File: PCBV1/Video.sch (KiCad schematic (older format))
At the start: 0 parts

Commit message: Made comments and some circuits.
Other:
- note added: "Place parallel LCD to HDMI circuits. \n\nBest option: TFP410\n\nPossible ICs:\nSI9022\nADV7513/ADV7511"
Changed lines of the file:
@@
 $Descr A4 11693 8268
 encoding utf-8
-Sheet 1 9
+Sheet 5 8
 Title "Smart Mirror"
 Date "2021-01-21"
@@
 Comment4 ""
 $EndDescr
+Text Notes 4650 3750 0    50   ~ 0
+Place parallel LCD to HDMI circuits. \n\nBest option: TFP410\n\nPossible ICs:\nSI9022\nADV7513/ADV7511
 $EndSCHEMATC

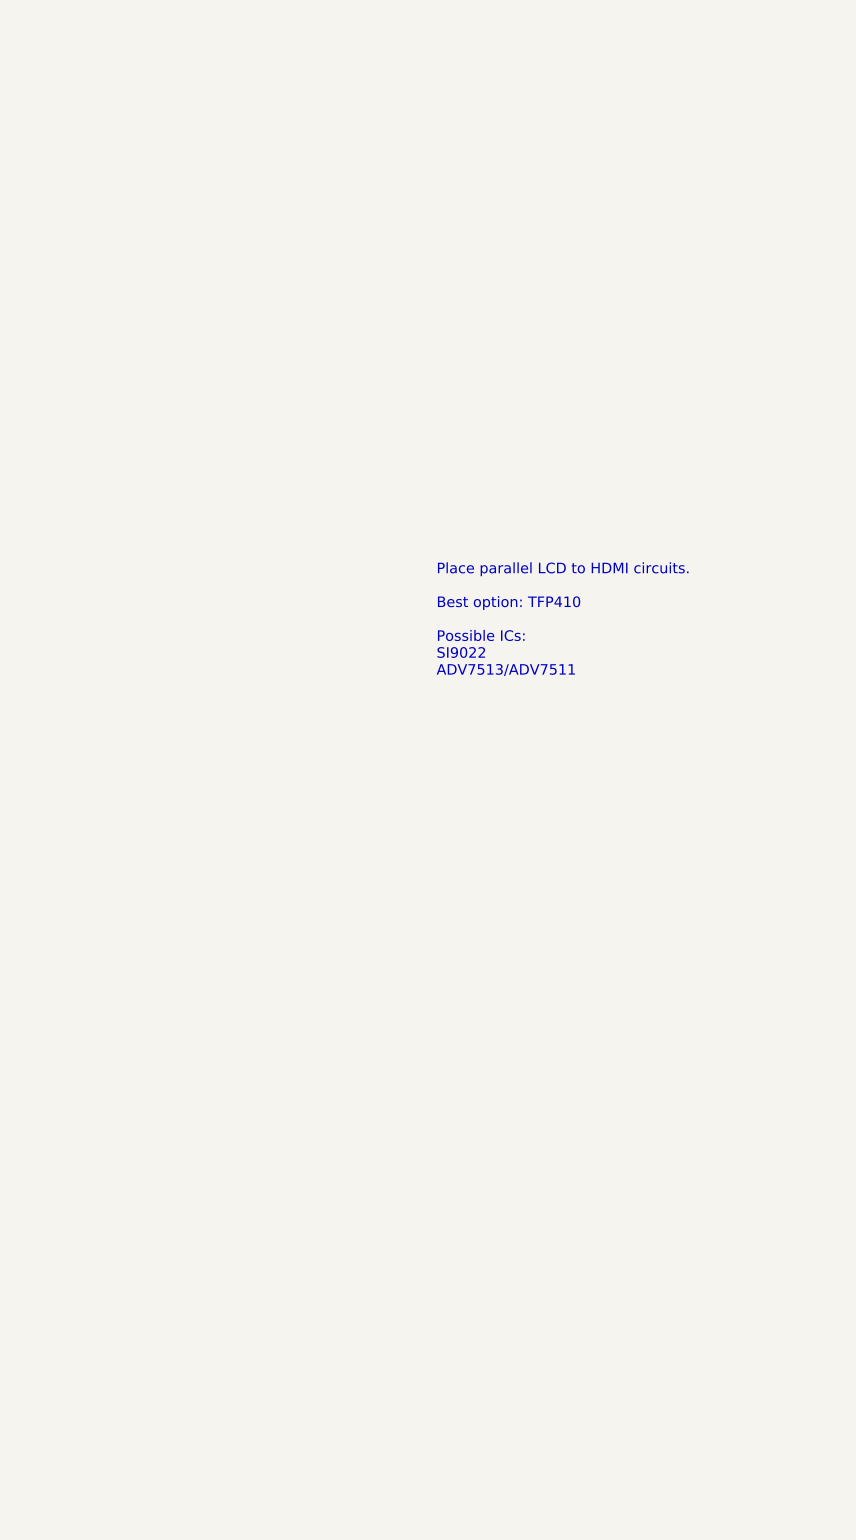
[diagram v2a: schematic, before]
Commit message: Added UART, modifications to video etc.
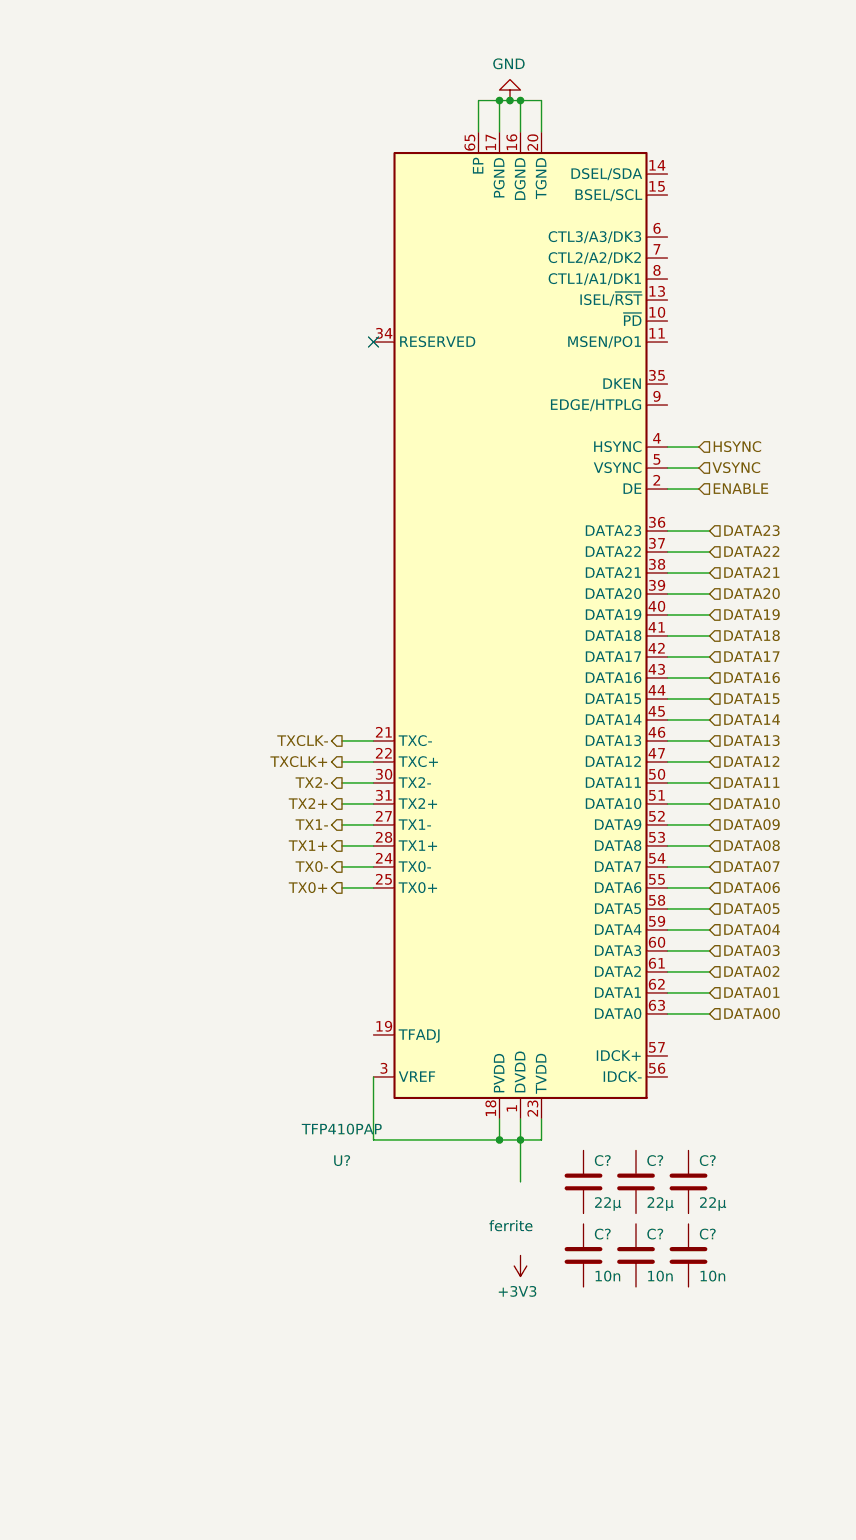
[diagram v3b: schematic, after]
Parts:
- added C? (x3): 22µ, symbol Device:C
- added C? (x3): 10n, symbol Device:C
- added U?: TFP410PAP, Package_QFP:HTQFP-64-1EP_10x10mm_P0.5mm_EP8x8mm_Mask4.4x4.4mm_ThermalVias, symbol Video:TFP410PAP
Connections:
- new net: U?.1 (DVDD), U?.12 (DVDD), U?.18 (PVDD), U?.23 (TVDD), U?.29 (TVDD), U?.3 (VREF), U?.33 (DVDD)
- new net DATA00: U?.63 (DATA0)
- new net DATA01: U?.62 (DATA1)
- new net DATA02: U?.61 (DATA2)
- new net DATA03: U?.60 (DATA3)
- new net DATA04: U?.59 (DATA4)
- new net DATA05: U?.58 (DATA5)
- new net DATA06: U?.55 (DATA6)
- new net DATA07: U?.54 (DATA7)
- new net DATA08: U?.53 (DATA8)
- new net DATA09: U?.52 (DATA9)
- new net DATA10: U?.51 (DATA10)
- new net DATA11: U?.50 (DATA11)
- new net DATA12: U?.47 (DATA12)
- new net DATA13: U?.46 (DATA13)
- new net DATA14: U?.45 (DATA14)
- new net DATA15: U?.44 (DATA15)
- new net DATA16: U?.43 (DATA16)
- new net DATA17: U?.42 (DATA17)
- new net DATA18: U?.41 (DATA18)
- new net DATA19: U?.40 (DATA19)
- new net DATA20: U?.39 (DATA20)
- new net DATA21: U?.38 (DATA21)
- new net DATA22: U?.37 (DATA22)
- new net DATA23: U?.36 (DATA23)
- new net ENABLE: U?.2 (DE)
- new net GND: U?.16 (DGND), U?.17 (PGND), U?.20 (TGND), U?.26 (TGND), U?.32 (TGND), U?.48 (DGND), U?.64 (DGND), U?.65 (EP)
- new net HSYNC: U?.4 (HSYNC)
- new net TX0+: U?.25 (TX0+)
- new net TX0-: U?.24 (TX0-)
- new net TX1+: U?.28 (TX1+)
- new net TX1-: U?.27 (TX1-)
- new net TX2+: U?.31 (TX2+)
- new net TX2-: U?.30 (TX2-)
- new net TXCLK+: U?.22 (TXC+)
- new net TXCLK-: U?.21 (TXC-)
- new net VSYNC: U?.5 (VSYNC)
- no-connect marks 0 -> 1
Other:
- note added: "ferrite"
- note removed: "Place parallel LCD to HDMI circuits. \n\nBest option: TFP410\n\nPossible ICs:\nSI9022\nADV7513/ADV7511"

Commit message: Finished video signals, added HDMI and SD connectors.
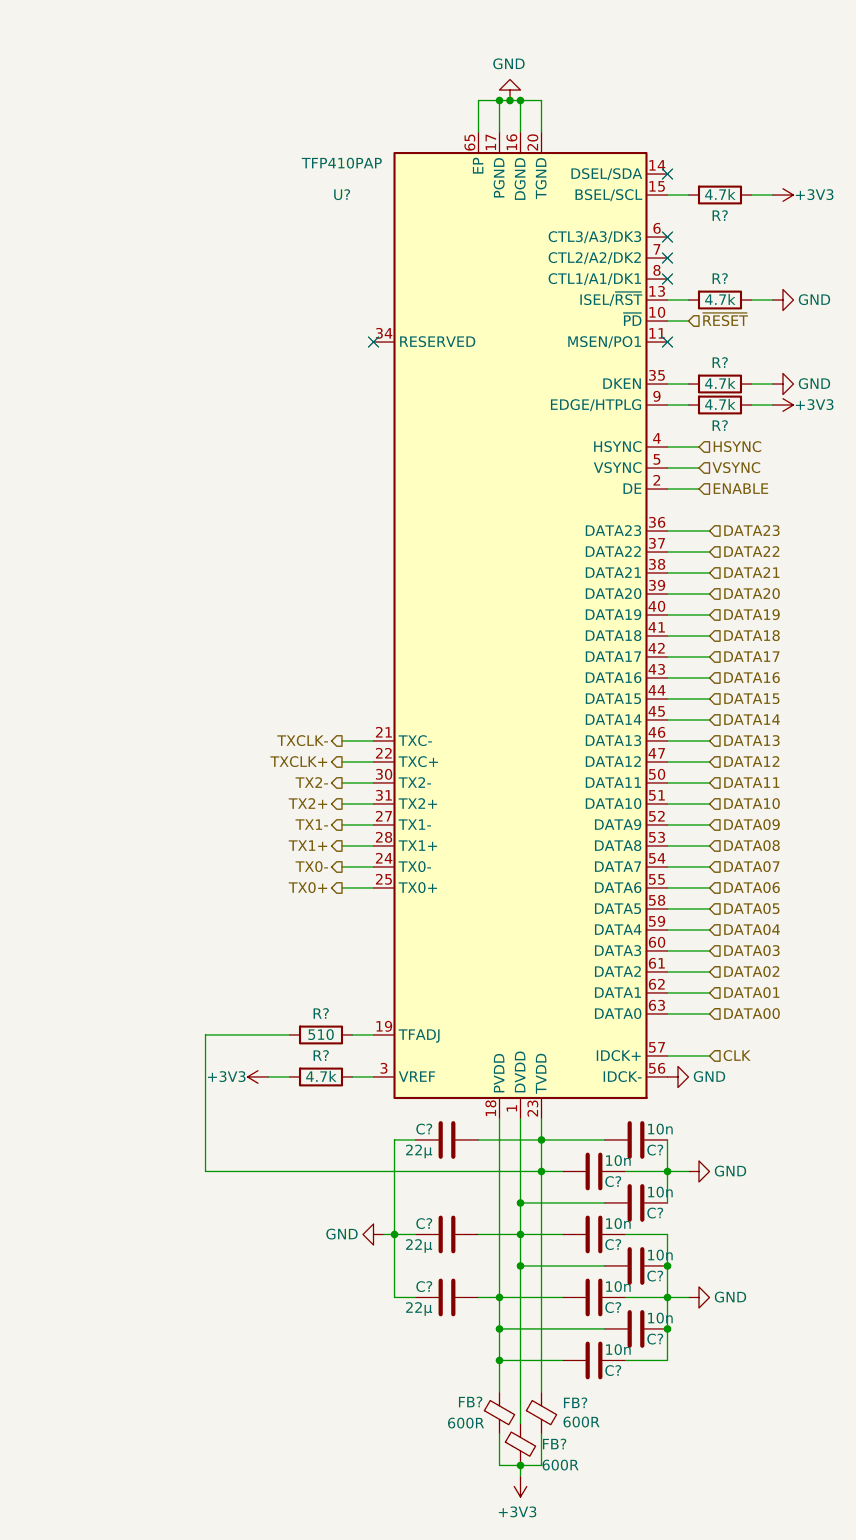
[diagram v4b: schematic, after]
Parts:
- removed C? (x2): 22µ, symbol Device:C
- removed C?: 10n, symbol Device:C
- added C? (x6): 10n, Capacitor_SMD:C_0603_1608Metric, symbol Device:C
- added C? (x2): 22µ, Capacitor_SMD:C_0603_1608Metric, symbol Device:C
- added FB? (x3): 600R, Inductor_SMD:L_0603_1608Metric, symbol Device:Ferrite_Bead_Small
- added R? (x5): 4.7k, Resistor_SMD:R_0603_1608Metric, symbol Device:R
- added R?: 510, Resistor_SMD:R_0603_1608Metric, symbol Device:R
- C? (x3): footprint (none) -> Capacitor_SMD:C_0603_1608Metric
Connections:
- net +3V3: now also FB?.2, FB?.2, FB?.2, R?.1, R?.1, R?.2
- net GND: now also C?.1, C?.1, C?.2, U?.56 (IDCK-), C?.1, C?.1, C?.1, C?.1, C?.1, C?.1, C?.2, C?.2, R?.1, R?.1
- net ~RESET: now reaches U?.10 (~PD)
- net at U?.13 (ISEL/~RST): now also R?.2
- net at U?.15 (BSEL/SCL): now also R?.2
- net at U?.19 (TFADJ): now also R?.1
- net at U?.35 (DKEN): now also R?.2
- net CLK: now reaches U?.57 (IDCK+)
- net at U?.9 (EDGE/HTPLG): now also R?.2
- net at C?.1: now also C?.2, U?.23 (TVDD), U?.29 (TVDD), C?.2, FB?.1, R?.2
- net at C?.2: now also U?.1 (DVDD), U?.12 (DVDD), U?.33 (DVDD), C?.1, C?.2, C?.2, FB?.1
- new net: C?.1, C?.2, C?.2, C?.2, FB?.1, U?.18 (PVDD)
- new net: R?.1, U?.3 (VREF)
- no-connect marks 1 -> 6
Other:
- note removed: "ferrite"
- moved on the sheet: C?

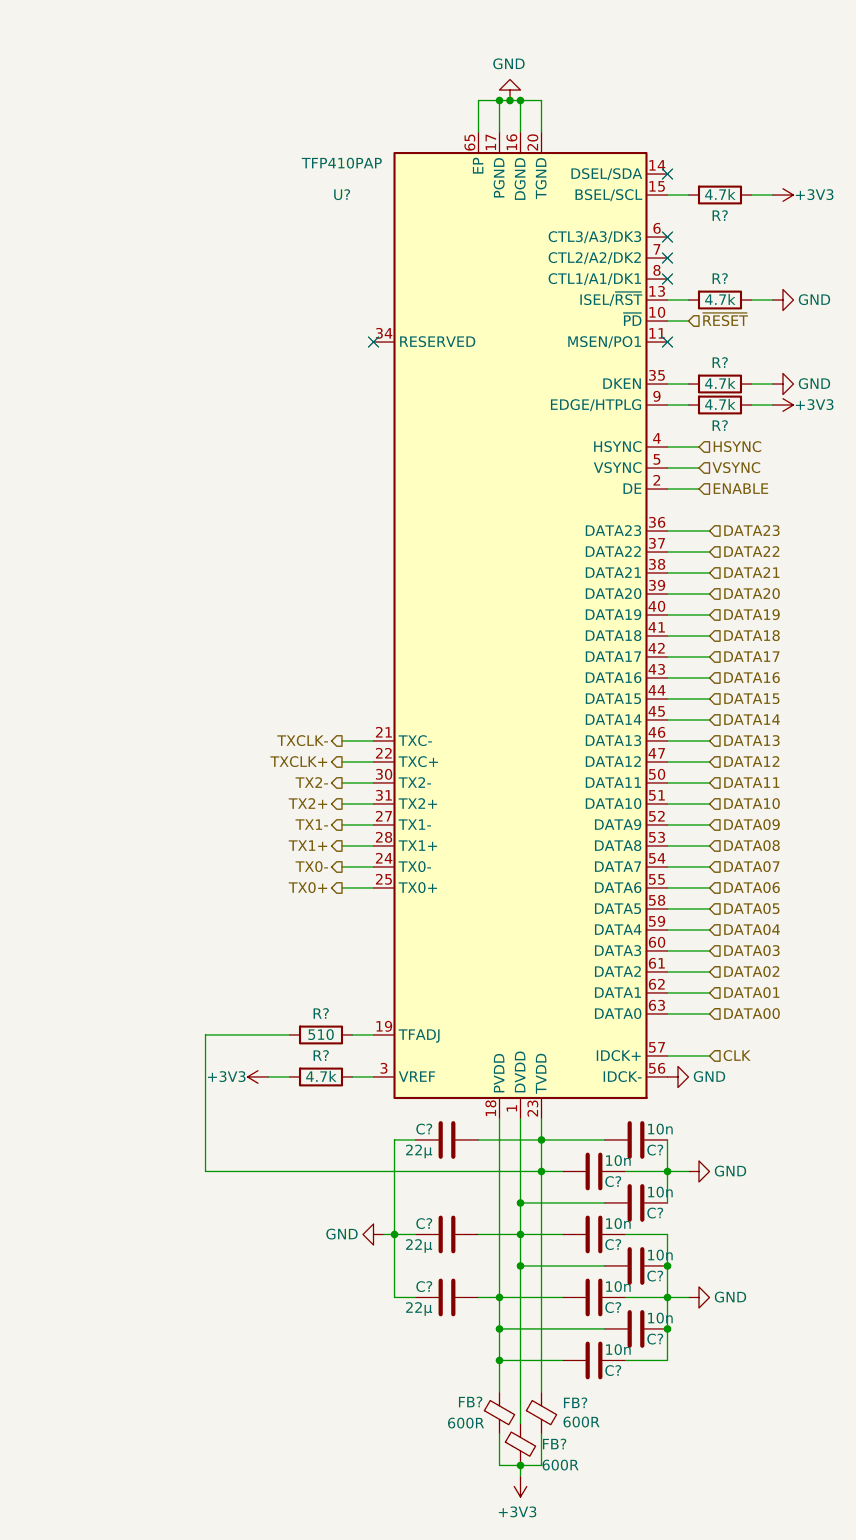
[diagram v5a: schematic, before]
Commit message: Many minor changes to component footprints and schematics.
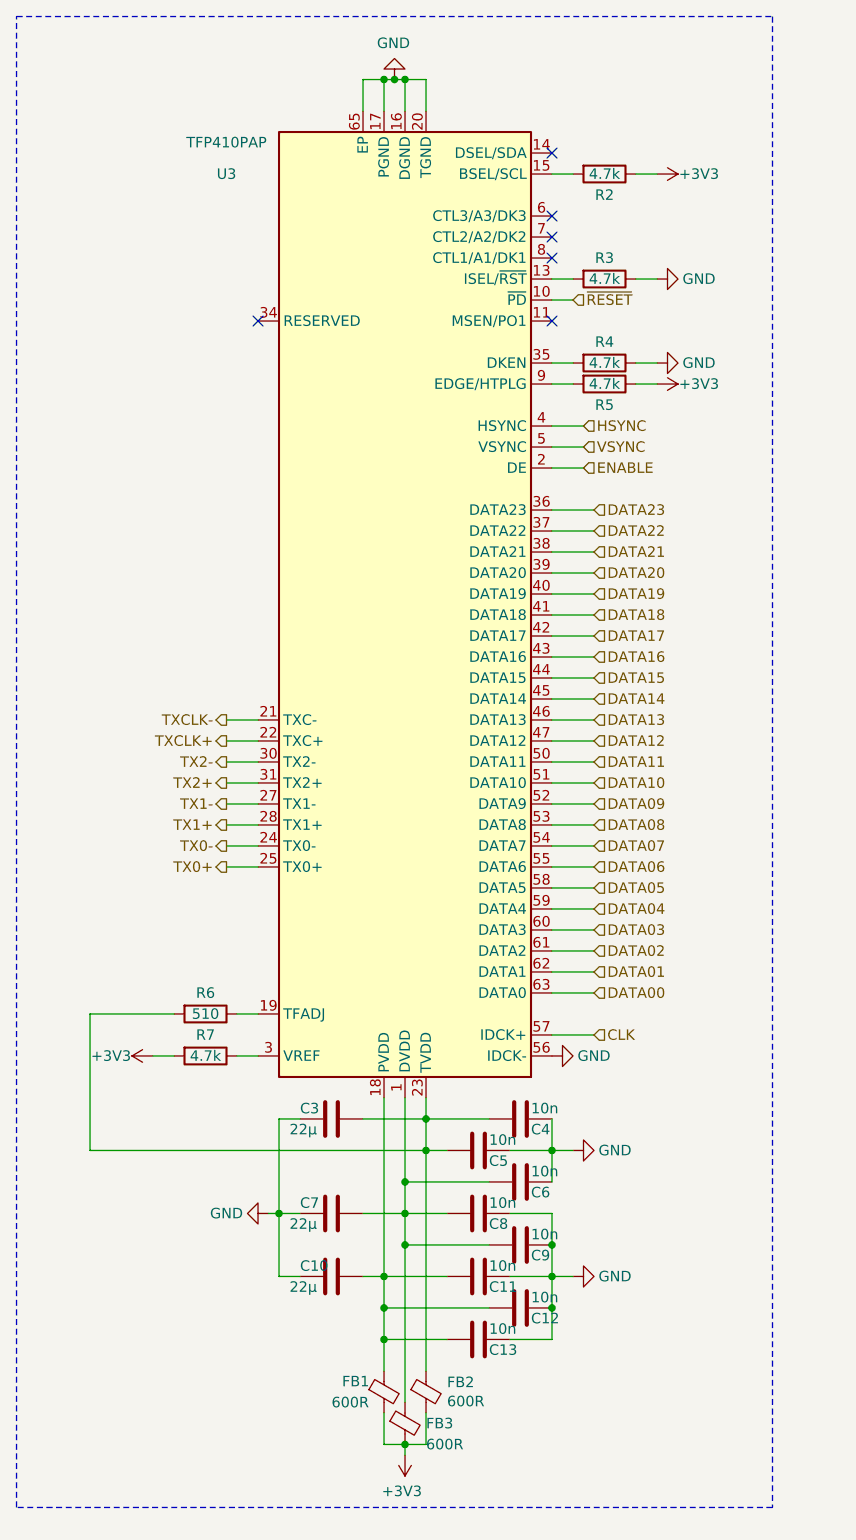
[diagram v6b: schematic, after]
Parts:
- gave numbers to parts that had none: 21
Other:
- moved on the sheet: C10, C11, C12, C13, C3, C4, C5, C6, C7, C8, C9, FB1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
